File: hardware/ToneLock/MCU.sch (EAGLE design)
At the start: 26 parts, among them U1 LD1117S33TR, U2 MP45DT02, U3 LIS3DSHTR, X3 MINI-USB-32005-201

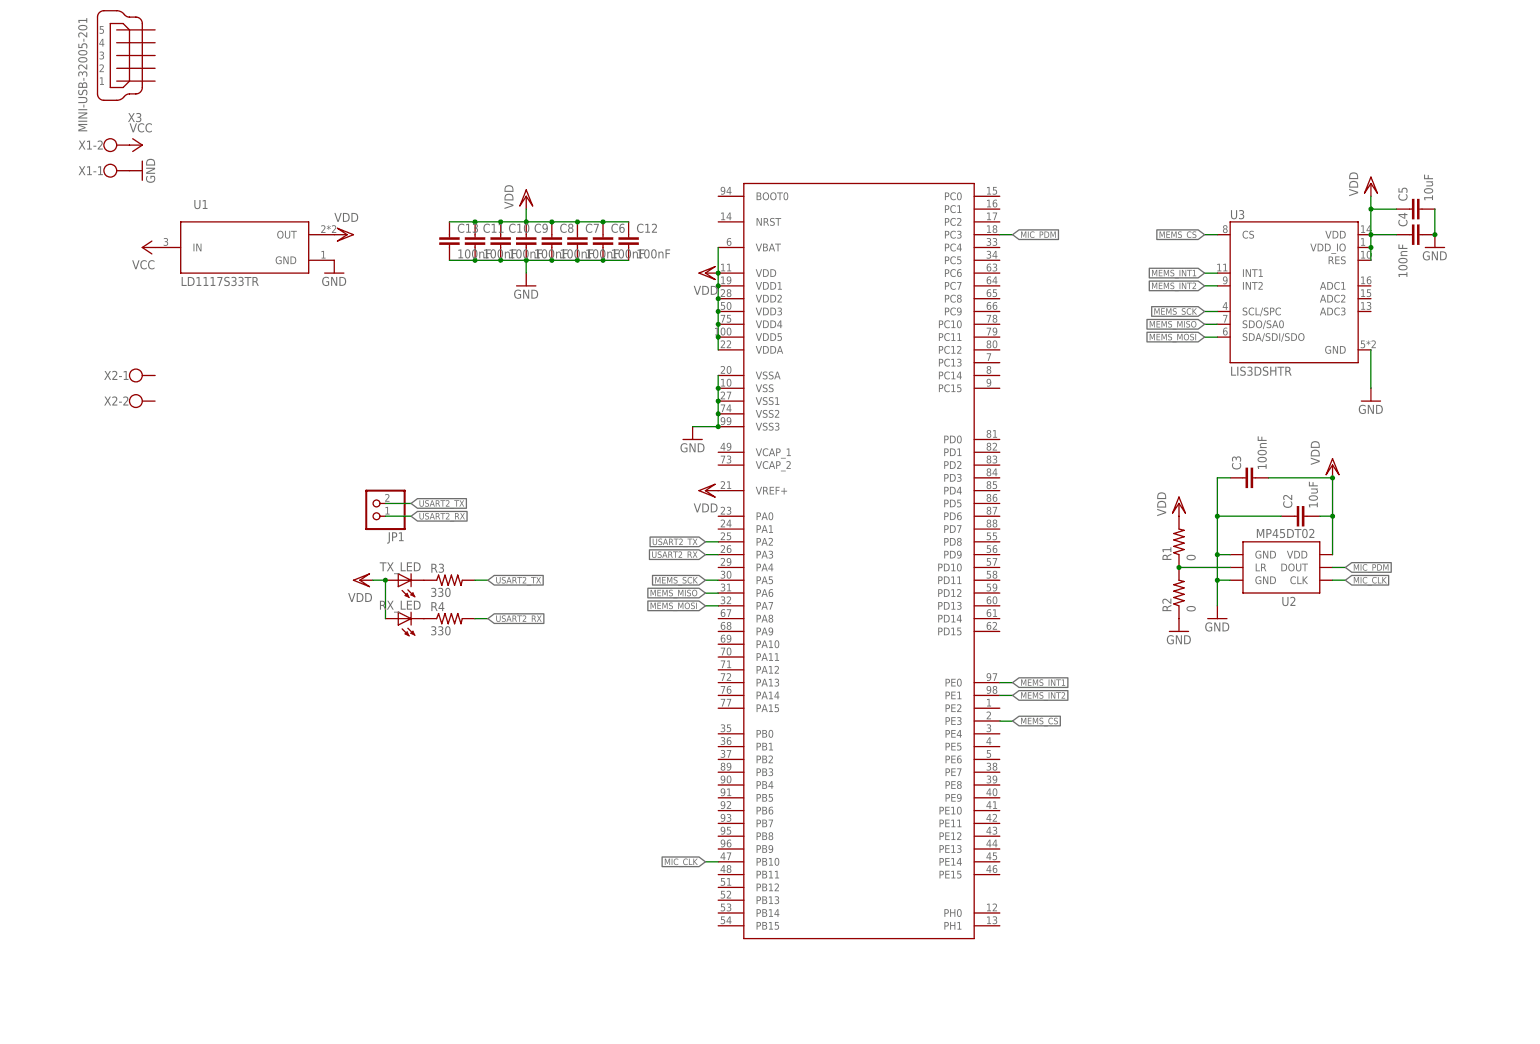
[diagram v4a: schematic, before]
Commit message: Added BOOT0 and NRST setups, power LED, Debugger
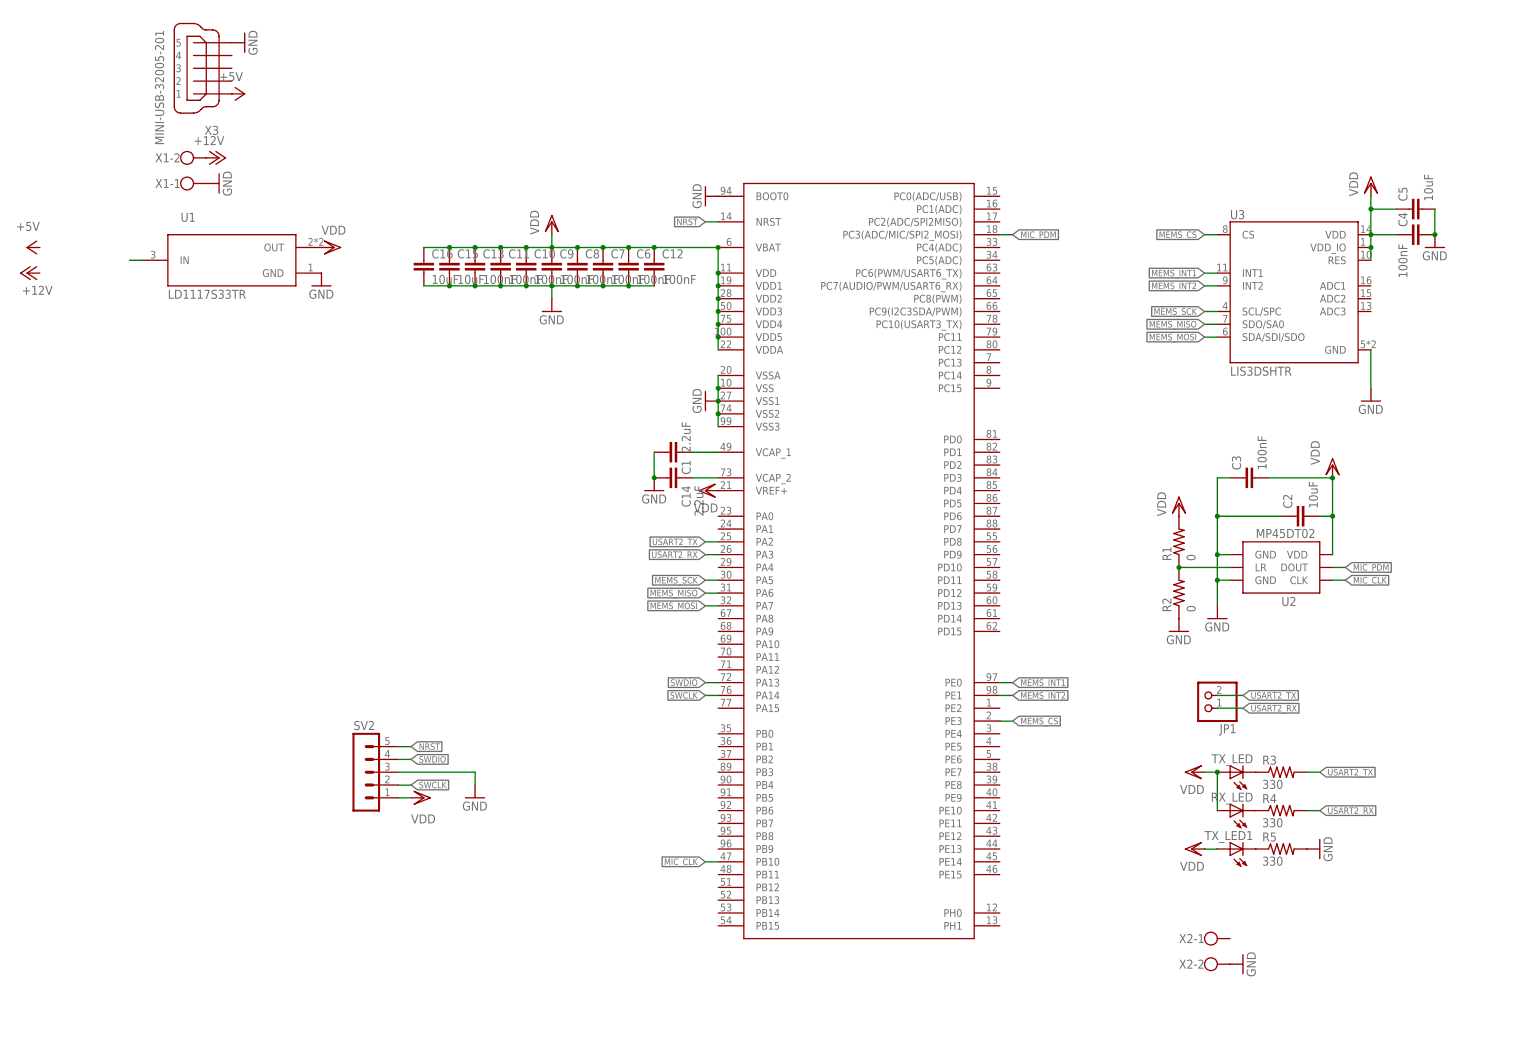
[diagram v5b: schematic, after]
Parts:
- added C1, C14: 2.2uF, resistor:C-EUC0603
- added C15, C16: 10uF, resistor:C-EUC0603
- added R5: 330, resistor:R-US_R0603
- added SV2: (no value), con-lstb:MA05-1
- added TX_LED1: (no value), led:LEDCHIP-LED0603
- U$1: value STM32F40XSTM32D40X -> STM32F407STM32D40X; device stm32f:STM32F40XSTM32D40X -> stm32f:STM32F407STM32D40X
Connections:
- removed net VCC: U1.IN, X1-2.KL
- new net +12V: X1-2.KL
- new net +5V: X3.1
- new net N$2: C14.1, U$1.VCAP_2
- new net N$5: C1.1, U$1.VCAP_1
- new net N$6: U1.IN
- new net N$7: R5.1, TX_LED1.C
- new net NRST: SV2.5, U$1.NRST
- new net SWCLK: SV2.2, U$1.PA14
- new net SWDIO: SV2.4, U$1.PA13
- net GND: now also C1.2, C14.2, C15.2, C16.2, R5.2, SV2.3, U$1.BOOT0, X2-2.KL, X3.5
- net MIC_PDM: now also U$1.PC3(ADC/MIC/SPI2_MOSI); no longer U$1.PC3
- net VDD: now also C15.1, C16.1, SV2.1, TX_LED1.A
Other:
- moved on the sheet: C10, C11, C12, C13, C6, C7, C8, C9, JP1, R3, R4, RX_LED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

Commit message: Completed schematic
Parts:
- removed TX_LED1: (no value), led:LEDCHIP-LED0603
- added D1, D2: BAT54C, diode:BAT54C
- added DBG_LED1, DBG_LED2, DBG_LED3, DBG_LED4, POWER_LED: (no value), led:LEDCHIP-LED0603
- added Q1: IRLML6346, bss138_10:IRLML6346
- added R11, R6, R7, R8: 330, resistor:R-EU_R0603
- added R9: 10k, resistor:R-EU_R0603
- R1, R2, R3, R4, R5: device resistor:R-US_R0603 -> resistor:R-EU_R0603
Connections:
- new net DBG_LED1: DBG_LED1.A, U$1.PD12
- new net DBG_LED2: DBG_LED2.A, U$1.PD13
- new net DBG_LED3: DBG_LED3.A, U$1.PD14
- new net DBG_LED4: DBG_LED4.A, U$1.PD15
- new net MOSFET_GATE: Q1.G, R9.2, U$1.PE2
- new net N$10: DBG_LED3.C, R6.1
- new net N$11: DBG_LED2.C, R7.1
- new net N$12: DBG_LED1.C, R8.1
- new net N$8: D2.CC, Q1.S, X2-1.KL
- new net N$9: DBG_LED4.C, R5.1
- net +12V: now also D1.A2, Q1.D
- net +5V: now also D1.A1
- net GND: now also D2.A1, D2.A2, R1.1, R11.2, R6.2, R7.2, R8.2, R9.1; no longer R2.1
- net N$1: now also POWER_LED.C, R11.1; no longer R3.1, TX_LED.C
- net N$3: now also R1.2, R2.1; no longer R1.1, R2.2
- net N$4: now also R3.1; no longer R4.1
- net N$6: now also D1.CC
- net N$7: now also R4.1, TX_LED.C; no longer R5.1, TX_LED1.C
- net USART2_RX: now also R3.2; no longer R4.2
- net USART2_TX: now also R4.2; no longer R3.2
- net VDD: now also POWER_LED.A, R2.2; no longer R1.2, TX_LED1.A
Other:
- moved on the sheet: C2, C3, C4, C5, JP1, RX_LED, SV2, TX_LED, U1, U2, U3, X1-1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

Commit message: Fixed MOSFET switch, grouped all components
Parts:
- added C17: 100nF, resistor:C-EUC0603
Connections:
- removed net N$8: D2.CC, Q1.S, X2-1.KL
- new net N$13: D2.A2, Q1.D, X2-2.KL
- net +12V: now also D2.CC, X2-1.KL; no longer Q1.D
- net GND: now also C17.2, Q1.S; no longer D2.A2, X2-2.KL
- net VDD: now also C17.1
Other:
- moved on the sheet: D2, X2-1, X2-2
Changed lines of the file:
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@@
 <part name="C15" library="resistor" library_urn="urn:adsk.eagle:library:348" deviceset="C-EU" device="C0603" package3d_urn="urn:adsk.eagle:package:23616/2" value="10uF"/>
 <part name="C16" library="resistor" library_urn="urn:adsk.eagle:library:348" deviceset="C-EU" device="C0603" package3d_urn="urn:adsk.eagle:package:23616/2" value="10uF"/>
-<part name="GND14" library="supply1" library_urn="urn:adsk.eagle:library:371" deviceset="GND" device=""/>
-<part name="P+5" library="supply1" library_urn="urn:adsk.eagle:library:371" deviceset="+12V" device=""/>
 <part name="DBG_LED1" library="led" library_urn="urn:adsk.eagle:library:259" deviceset="LED" device="CHIP-LED0603" package3d_urn="urn:adsk.eagle:package:15819/3"/>
 <part name="GND15" library="supply1" library_urn="urn:adsk.eagle:library:371" deviceset="GND" device=""/>
@@
 <part name="R9" library="resistor" library_urn="urn:adsk.eagle:library:348" deviceset="R-EU_" device="R0603" package3d_urn="urn:adsk.eagle:package:23555/2" value="10k"/>
 <part name="Q1" library="bss138_10" deviceset="IRLML6346" device=""/>
+<part name="GND21" library="supply1" library_urn="urn:adsk.eagle:library:371" deviceset="GND" device=""/>
+<part name="P+5" library="supply1" library_urn="urn:adsk.eagle:library:371" deviceset="+12V" device=""/>
+<part name="C17" library="resistor" library_urn="urn:adsk.eagle:library:348" deviceset="C-EU" device="C0603" package3d_urn="urn:adsk.eagle:package:23616/2" value="100nF"/>
 </parts>
 <sheets>
@@
 <instance part="RX_LED" gate="G$1" x="96.52" y="35.56" rot="R90"/>
 <instance part="VDD8" gate="G$1" x="88.9" y="43.18" rot="R90"/>
-<instance part="X2" gate="-1" x="129.54" y="5.08" smashed="yes" rot="R180">
-<attribute name="NAME" x="132.08" y="4.191" size="1.778" layer="95"/>
-</instance>
-<instance part="X2" gate="-2" x="129.54" y="0" smashed="yes" rot="R180">
-<attribute name="VALUE" x="132.08" y="3.683" size="1.778" layer="96" rot="R180"/>
-<attribute name="NAME" x="132.08" y="-0.889" size="1.778" layer="95"/>
+<instance part="X2" gate="-1" x="91.44" y="0" smashed="yes">
+<attribute name="NAME" x="88.9" y="0.889" size="1.778" layer="95" rot="R180"/>
+</instance>
+<instance part="X2" gate="-2" x="91.44" y="5.08" smashed="yes">
+<attribute name="VALUE" x="88.9" y="1.397" size="1.778" layer="96"/>
+<attribute name="NAME" x="88.9" y="5.969" size="1.778" layer="95" rot="R180"/>
 </instance>
 <instance part="GND8" gate="1" x="-55.88" y="88.9" rot="R90"/>
@@
 <instance part="C15" gate="G$1" x="-58.42" y="134.62"/>
 <instance part="C16" gate="G$1" x="-63.5" y="134.62"/>
-<instance part="GND14" gate="1" x="121.92" y="-2.54" smashed="yes">
-<attribute name="VALUE" x="124.46" y="-5.08" size="1.778" layer="96" rot="R180"/>
-</instance>
-<instance part="P+5" gate="1" x="99.06" y="5.08" rot="R90"/>
 <instance part="DBG_LED1" gate="G$1" x="137.16" y="73.66" rot="R90"/>
 <instance part="GND15" gate="1" x="152.4" y="71.12"/>
@@
 <instance part="GND19" gate="1" x="111.76" y="-15.24"/>
 <instance part="D1" gate="G$1" x="-73.66" y="73.66" rot="R270"/>
-<instance part="D2" gate="G$1" x="121.92" y="5.08" smashed="yes" rot="R270">
-<attribute name="NAME" x="117.602" y="2.0066" size="1.778" layer="95"/>
-<attribute name="VALUE" x="125.222" y="8.7376" size="1.778" layer="96"/>
-</instance>
-<instance part="GND20" gate="1" x="121.92" y="12.7" rot="R180"/>
+<instance part="D2" gate="G$1" x="99.06" y="0" smashed="yes" rot="R90">
+<attribute name="NAME" x="103.378" y="3.0734" size="1.778" layer="95" rot="R180"/>
+<attribute name="VALUE" x="95.758" y="-3.6576" size="1.778" layer="96" rot="R180"/>
+</instance>
+<instance part="GND20" gate="1" x="99.06" y="-7.62"/>
 <instance part="R11" gate="G$1" x="106.68" y="27.94"/>
 <instance part="R3" gate="G$1" x="106.68" y="35.56"/>
@@
 <instance part="R9" gate="G$1" x="111.76" y="-7.62" rot="R90"/>
 <instance part="Q1" gate="G$1" x="109.22" y="2.54" smashed="yes" rot="R90">
-<attribute name="VALUE" x="110.49" y="10.16" size="1.778" layer="96" rot="R180"/>
-<attribute name="NAME" x="115.57" y="7.62" size="1.778" layer="95" rot="R180"/>
-</instance>
+<attribute name="VALUE" x="118.11" y="10.16" size="1.778" layer="96" rot="R180"/>
+<attribute name="NAME" x="110.49" y="0" size="1.778" layer="95" rot="R180"/>
+</instance>
+<instance part="GND21" gate="1" x="116.84" y="5.08" rot="R90"/>
+<instance part="P+5" gate="1" x="104.14" y="0" smashed="yes" rot="R270">
+<attribute name="VALUE" x="101.6" y="-2.54" size="1.778" layer="96"/>
+</instance>
+<instance part="C17" gate="G$1" x="-68.58" y="134.62"/>
 </instances>
 <busses>
@@
 <wire x1="-58.42" y1="129.54" x2="-63.5" y2="129.54" width="0.1524" layer="91"/>
 <junction x="-58.42" y="129.54"/>
+<pinref part="C17" gate="G$1" pin="2"/>
+<wire x1="-68.58" y1="129.54" x2="-63.5" y2="129.54" width="0.1524" layer="91"/>
+<junction x="-63.5" y="129.54"/>
 </segment>
 <segment>
@@
 </segment>
 <segment>
-<pinref part="X2" gate="-2" pin="KL"/>
-<pinref part="GND14" gate="1" pin="GND"/>
-<pinref part="GND14" gate="1" pin="GND"/>
-<wire x1="121.92" y1="0" x2="124.46" y2="0" width="0.1524" layer="91"/>
-<junction x="121.92" y="0"/>
-<pinref part="D2" gate="G$1" pin="A2"/>
-</segment>
-<segment>
 <pinref part="D2" gate="G$1" pin="A1"/>
 <pinref part="GND20" gate="1" pin="GND"/>
@@
 <pinref part="GND19" gate="1" pin="GND"/>
 <pinref part="R9" gate="G$1" pin="1"/>
+</segment>
+<segment>
+<pinref part="Q1" gate="G$1" pin="S"/>
+<pinref part="GND21" gate="1" pin="GND"/>
 </segment>
 </net>
@@
 <wire x1="-58.42" y1="137.16" x2="-63.5" y2="137.16" width="0.1524" layer="91"/>
 <junction x="-58.42" y="137.16"/>
+<pinref part="C17" gate="G$1" pin="1"/>
+<wire x1="-68.58" y1="137.16" x2="-63.5" y2="137.16" width="0.1524" layer="91"/>
+<junction x="-63.5" y="137.16"/>
 </segment>
 <segment>
@@
 </segment>
 <segment>
-<pinref part="P+5" gate="1" pin="+12V"/>
-<wire x1="101.6" y1="5.08" x2="104.14" y2="5.08" width="0.1524" layer="91"/>
-<pinref part="Q1" gate="G$1" pin="D"/>
-</segment>
-<segment>
 <pinref part="P+4" gate="1" pin="+12V"/>
 <pinref part="D1" gate="G$1" pin="A2"/>
+</segment>
+<segment>
+<pinref part="X2" gate="-1" pin="KL"/>
+<pinref part="D2" gate="G$1" pin="CC"/>
+<pinref part="P+5" gate="1" pin="+12V"/>
+<wire x1="101.6" y1="0" x2="96.52" y2="0" width="0.1524" layer="91"/>
+<junction x="96.52" y="0"/>
 </segment>
 </net>
@@
 </segment>
 <segment>
-<label x="111.76" y="-2.54" size="1.27" layer="95" rot="R180" xref="yes"/>
+<label x="111.76" y="-2.54" size="1.27" layer="95" xref="yes"/>
 <wire x1="111.76" y1="-2.54" x2="111.76" y2="0" width="0.1524" layer="91"/>
 <pinref part="R9" gate="G$1" pin="2"/>
@@
 </segment>
 </net>
-<net name="N$8" class="0">
-<segment>
-<pinref part="X2" gate="-1" pin="KL"/>
-<pinref part="D2" gate="G$1" pin="CC"/>
-<wire x1="114.3" y1="5.08" x2="124.46" y2="5.08" width="0.1524" layer="91"/>
-<junction x="124.46" y="5.08"/>
-<pinref part="Q1" gate="G$1" pin="S"/>
-</segment>
-</net>
 <net name="N$1" class="0">
 <segment>
@@
 </segment>
 </net>
+<net name="N$13" class="0">
+<segment>
+<pinref part="X2" gate="-2" pin="KL"/>
+<wire x1="99.06" y1="5.08" x2="96.52" y2="5.08" width="0.1524" layer="91"/>
+<pinref part="D2" gate="G$1" pin="A2"/>
+<pinref part="Q1" gate="G$1" pin="D"/>
+<wire x1="99.06" y1="5.08" x2="104.14" y2="5.08" width="0.1524" layer="91"/>
+<junction x="99.06" y="5.08"/>
+</segment>
+</net>
